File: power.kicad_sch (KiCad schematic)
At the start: 22 parts, among them U5 LMR50410YFQDBVRQ1, U6 LMR50410YFQDBVRQ1

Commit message: did some stuff yesterday i dont remember
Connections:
- net +24V renamed Vin

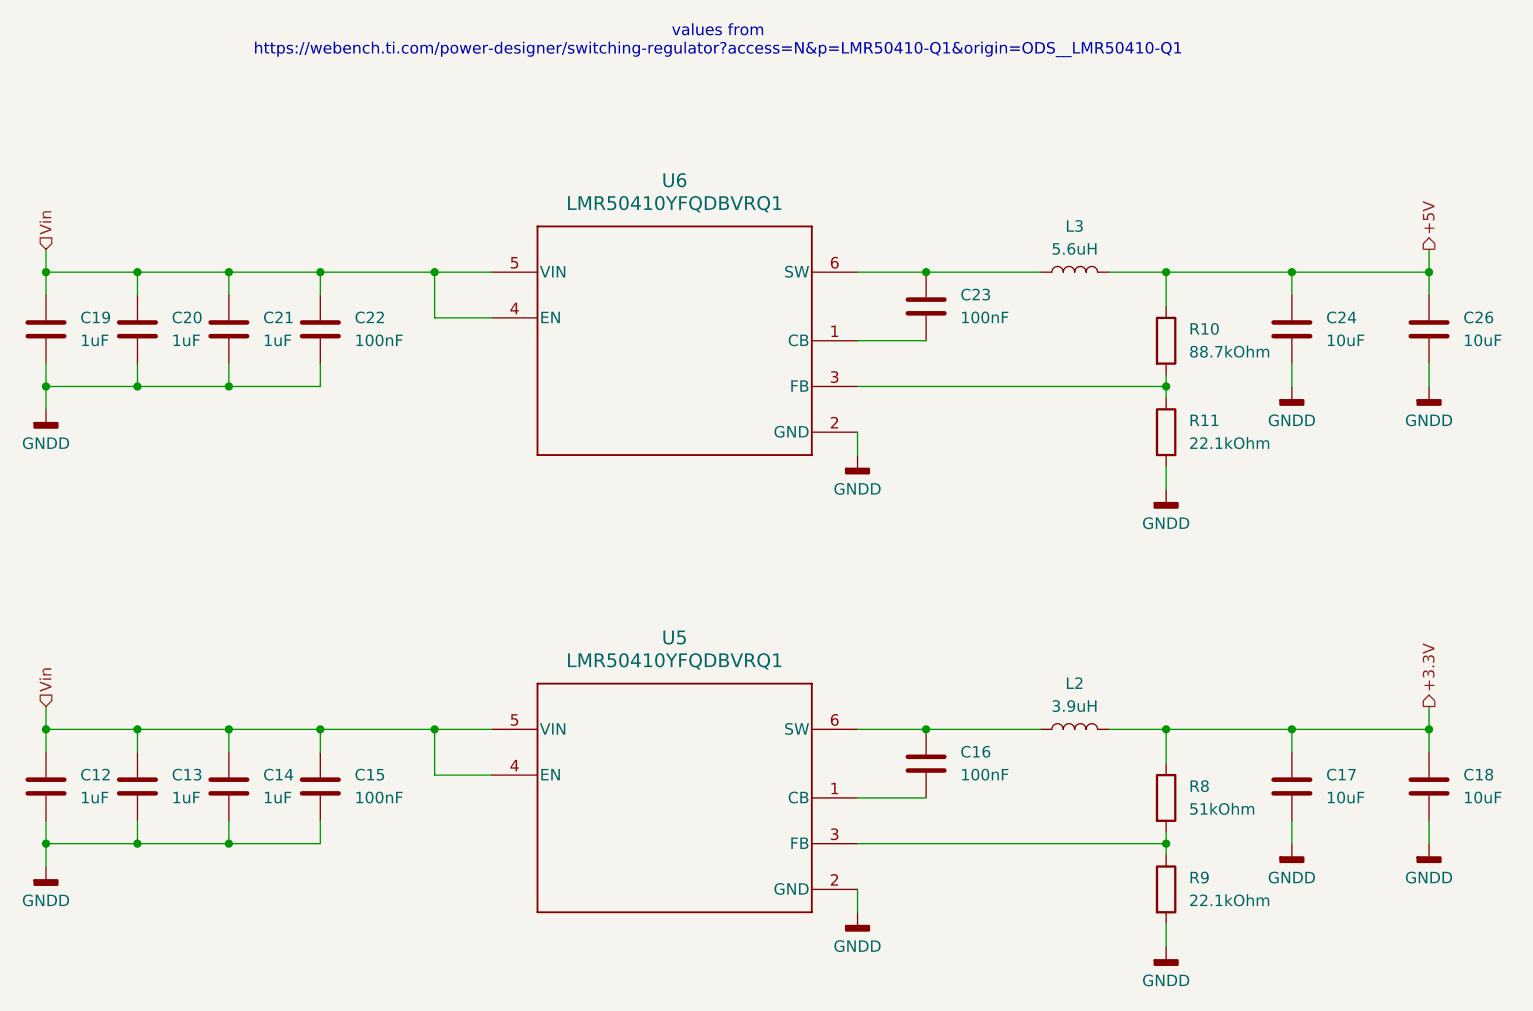
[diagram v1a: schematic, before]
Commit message: assigned footprints, some minor schematic stuff, started layout
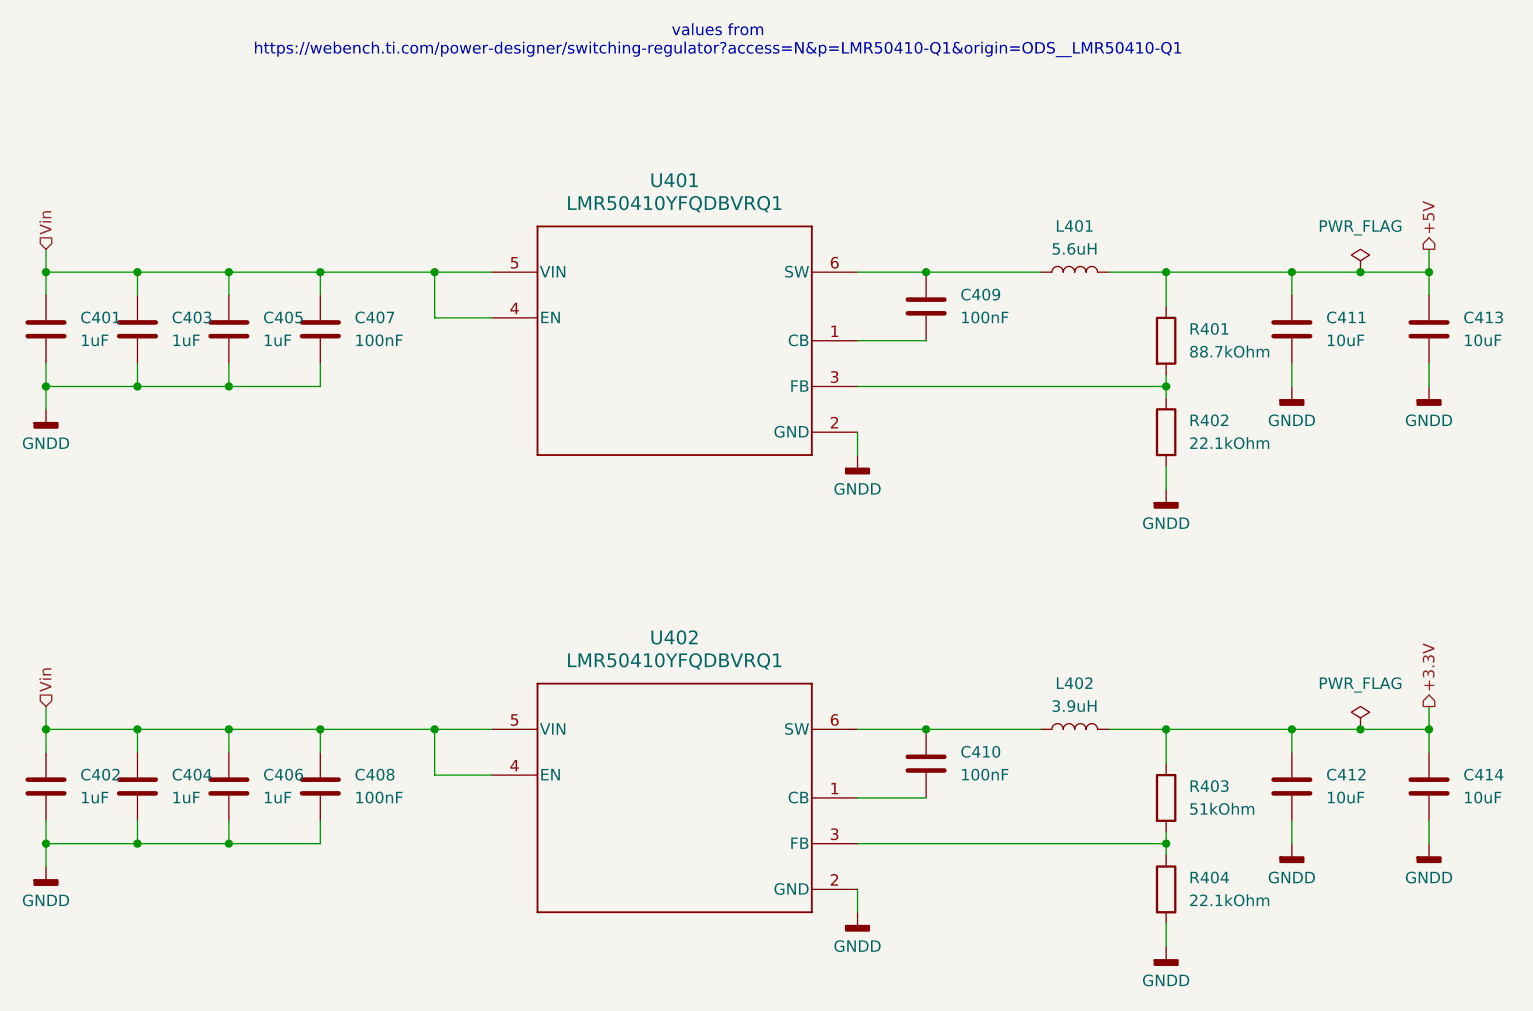
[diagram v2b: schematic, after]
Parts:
- C401: renamed from C19; footprint (none) -> Capacitor_SMD:C_0603_1608Metric
- C402: renamed from C12; footprint (none) -> Capacitor_SMD:C_0603_1608Metric
- C403: renamed from C20; footprint (none) -> Capacitor_SMD:C_0603_1608Metric
- C404: renamed from C13; footprint (none) -> Capacitor_SMD:C_0603_1608Metric
- C405: renamed from C21; footprint (none) -> Capacitor_SMD:C_0603_1608Metric
- C406: renamed from C14; footprint (none) -> Capacitor_SMD:C_0603_1608Metric
- C407: renamed from C22; footprint (none) -> Capacitor_SMD:C_0603_1608Metric
- C408: renamed from C15; footprint (none) -> Capacitor_SMD:C_0603_1608Metric
- C409: renamed from C23; footprint (none) -> Capacitor_SMD:C_0603_1608Metric
- C410: renamed from C16; footprint (none) -> Capacitor_SMD:C_0603_1608Metric
- C411: renamed from C24; footprint (none) -> Capacitor_SMD:C_0603_1608Metric
- C412: renamed from C17; footprint (none) -> Capacitor_SMD:C_0603_1608Metric
- C413: renamed from C26; footprint (none) -> Capacitor_SMD:C_0603_1608Metric
- C414: renamed from C18; footprint (none) -> Capacitor_SMD:C_0603_1608Metric
- L401: renamed from L3; footprint (none) -> Inductor_SMD:L_1812_4532Metric
- L402: renamed from L2; footprint (none) -> Inductor_SMD:L_1812_4532Metric
- R401: renamed from R10; footprint (none) -> Resistor_SMD:R_0603_1608Metric
- R402: renamed from R11; footprint (none) -> Resistor_SMD:R_0603_1608Metric
- R403: renamed from R8; footprint (none) -> Resistor_SMD:R_0603_1608Metric
- R404: renamed from R9; footprint (none) -> Resistor_SMD:R_0603_1608Metric
- U401: renamed from U6; footprint DBV0006A-IPC_A -> footprints:DBV0006A-IPC_A
- U402: renamed from U5; footprint DBV0006A-IPC_A -> footprints:DBV0006A-IPC_A

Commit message: Layout done except for silkscreen
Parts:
- C401, C402, C403, C404, C405, C406, C411, C412, C413, C414: footprint Capacitor_SMD:C_0603_1608Metric -> Capacitor_SMD:C_1206_3216Metric
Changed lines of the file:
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@@
 			)
 		)
-		(property "Footprint" "Capacitor_SMD:C_0603_1608Metric"
+		(property "Footprint" "Capacitor_SMD:C_1206_3216Metric"
 			(at 73.3552 69.85 0)
 			(hide yes)
@@
 			)
 		)
-		(property "Footprint" "Capacitor_SMD:C_0603_1608Metric"
+		(property "Footprint" "Capacitor_SMD:C_1206_3216Metric"
 			(at 93.6752 120.65 0)
 			(hide yes)
@@
 			)
 		)
-		(property "Footprint" "Capacitor_SMD:C_0603_1608Metric"
+		(property "Footprint" "Capacitor_SMD:C_1206_3216Metric"
 			(at 83.5152 69.85 0)
 			(hide yes)
@@
 			)
 		)
-		(property "Footprint" "Capacitor_SMD:C_0603_1608Metric"
+		(property "Footprint" "Capacitor_SMD:C_1206_3216Metric"
 			(at 211.7852 120.65 0)
 			(hide yes)
@@
 			)
 		)
-		(property "Footprint" "Capacitor_SMD:C_0603_1608Metric"
+		(property "Footprint" "Capacitor_SMD:C_1206_3216Metric"
 			(at 211.7852 69.85 0)
 			(hide yes)
@@
 			)
 		)
-		(property "Footprint" "Capacitor_SMD:C_0603_1608Metric"
+		(property "Footprint" "Capacitor_SMD:C_1206_3216Metric"
 			(at 73.3552 120.65 0)
 			(hide yes)
@@
 			)
 		)
-		(property "Footprint" "Capacitor_SMD:C_0603_1608Metric"
+		(property "Footprint" "Capacitor_SMD:C_1206_3216Metric"
 			(at 227.0252 69.85 0)
 			(hide yes)
@@
 			)
 		)
-		(property "Footprint" "Capacitor_SMD:C_0603_1608Metric"
+		(property "Footprint" "Capacitor_SMD:C_1206_3216Metric"
 			(at 227.0252 120.65 0)
 			(hide yes)
@@
 			)
 		)
-		(property "Footprint" "Capacitor_SMD:C_0603_1608Metric"
+		(property "Footprint" "Capacitor_SMD:C_1206_3216Metric"
 			(at 83.5152 120.65 0)
 			(hide yes)
@@
 			)
 		)
-		(property "Footprint" "Capacitor_SMD:C_0603_1608Metric"
+		(property "Footprint" "Capacitor_SMD:C_1206_3216Metric"
 			(at 93.6752 69.85 0)
 			(hide yes)
